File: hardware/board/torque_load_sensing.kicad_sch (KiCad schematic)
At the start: 35 parts

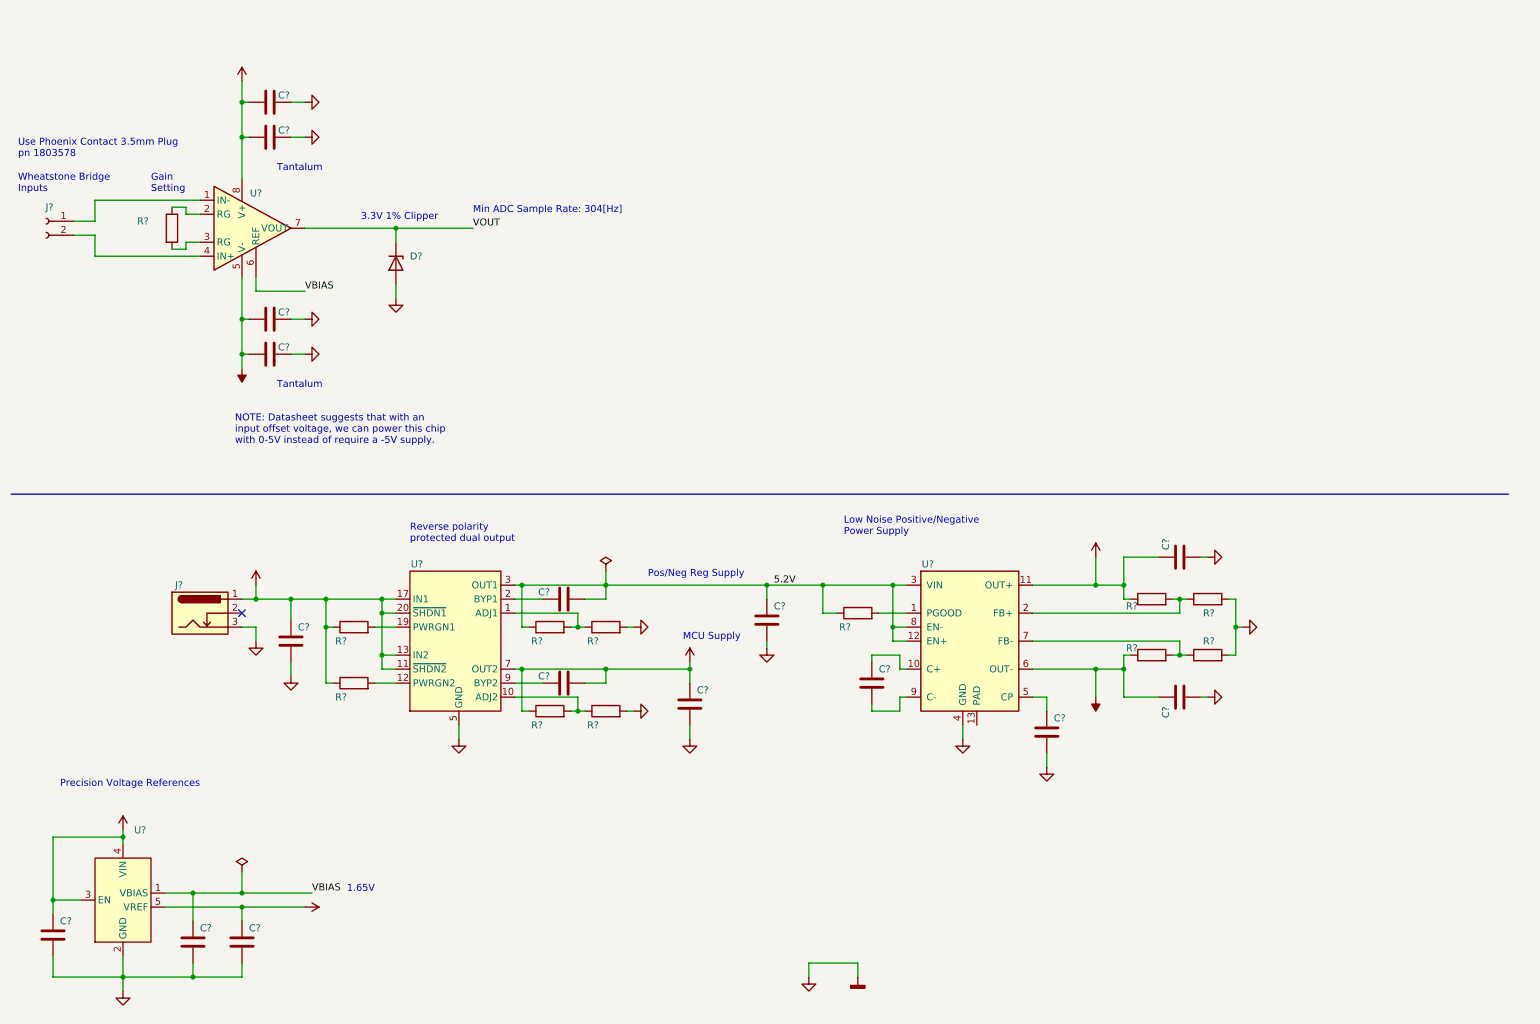
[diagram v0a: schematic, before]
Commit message: adc reading works
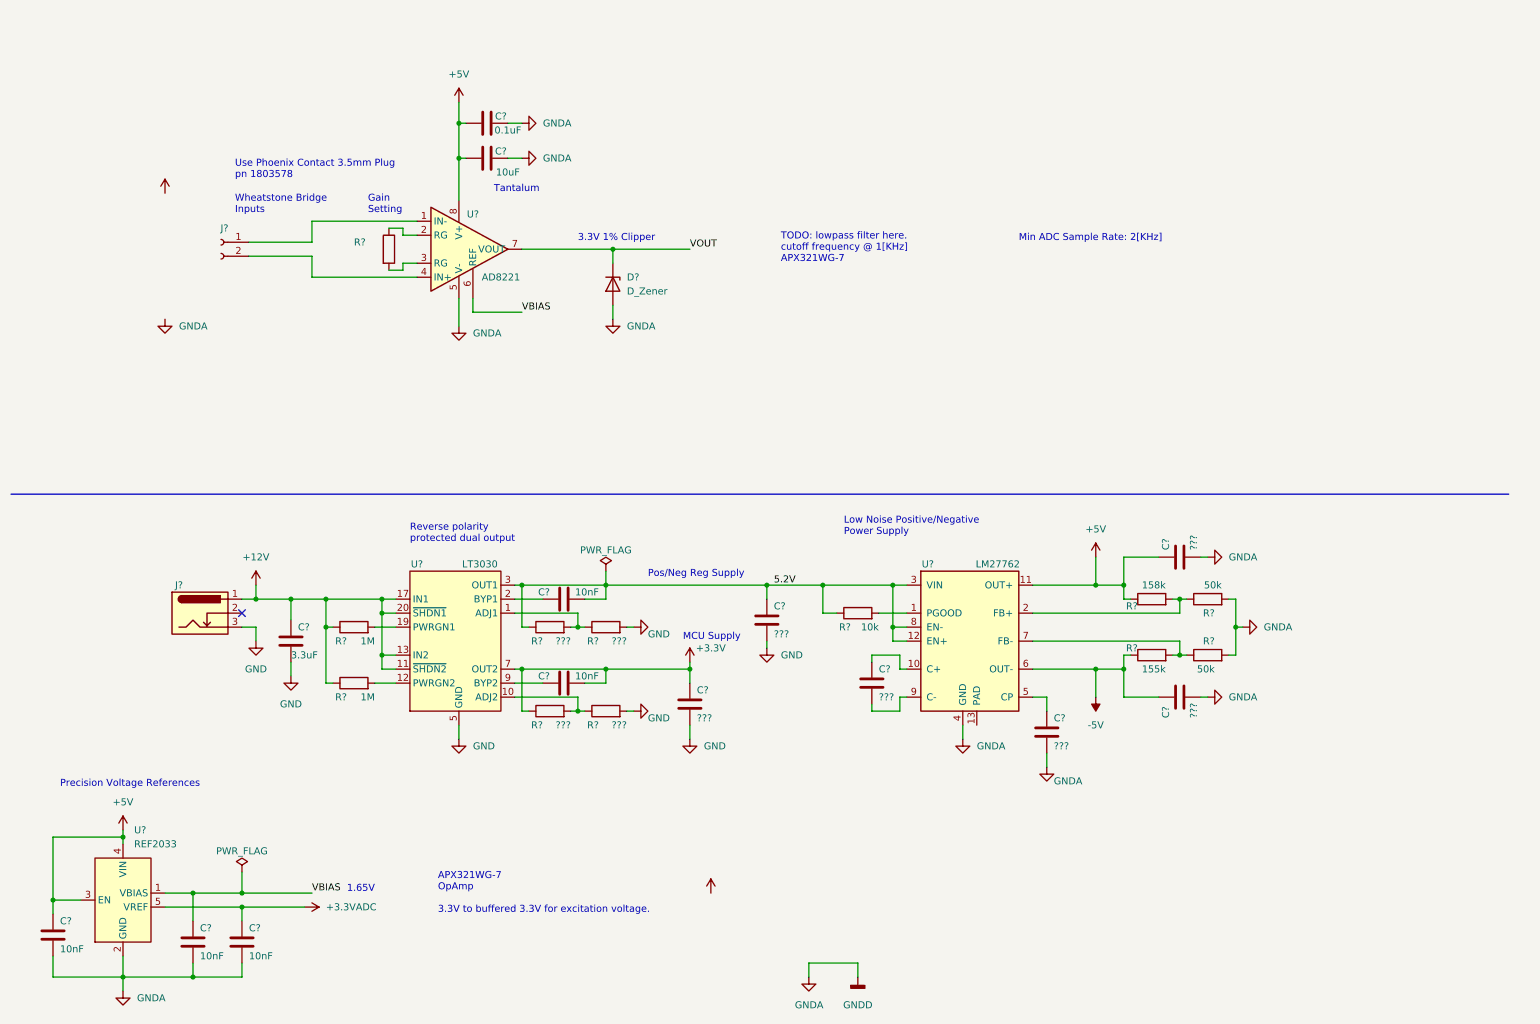
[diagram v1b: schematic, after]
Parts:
- removed C? (x2): (no value), symbol Device:C
- C? (x6), R? (x4): value (none) -> ???
- C? (x5): value (none) -> 10nF
- C?: value (none) -> 0.1uF
- C?: value (none) -> 10uF
- C?: value (none) -> 3.3uF
- D?: value (none) -> D_Zener
- J?: value (none) -> Conn_01x02_Female
- J?: value (none) -> Barrel_Jack_Switch_Pin3Ring
- R?: value (none) -> 155k
- R?: value (none) -> 158k
- R? (x2): value (none) -> 50k
- R?: value (none) -> 10k
- R? (x2): value (none) -> 1M
- U?: value (none) -> AD8221; footprint (none) -> Package_SO:MSOP-8_3x3mm_P0.65mm
- U?: value (none) -> REF2033; footprint (none) -> Package_TO_SOT_SMD:SOT-23-5
- U?: value (none) -> LT3030
- U?: value (none) -> LM27762; footprint (none) -> Package_SON:WSON-12-1EP_3x2mm_P0.5mm_EP1x2.65_ThermalVias
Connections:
- net -5V: no longer U?.5 (V-)
- net GNDA: now also U?.5 (V-)
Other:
- note added: "APX321WG-7 OpAmp 3.3V to buffered 3.3V for excitation voltage."
- note added: "Min ADC Sample Rate: 2[KHz]"
- note added: "TODO: lowpass filter here. cutoff frequency @ 1[KHz] APX321WG-7"
- note removed: "Min ADC Sample Rate: 304[Hz]"
- note removed: "NOTE: Datasheet suggests that with an input offset voltage, we can power this chip with 0-5V instead of require a -5V supply."
- moved on the sheet: C?, D?, J?, R?, U?

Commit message: debug port works; draft current driver
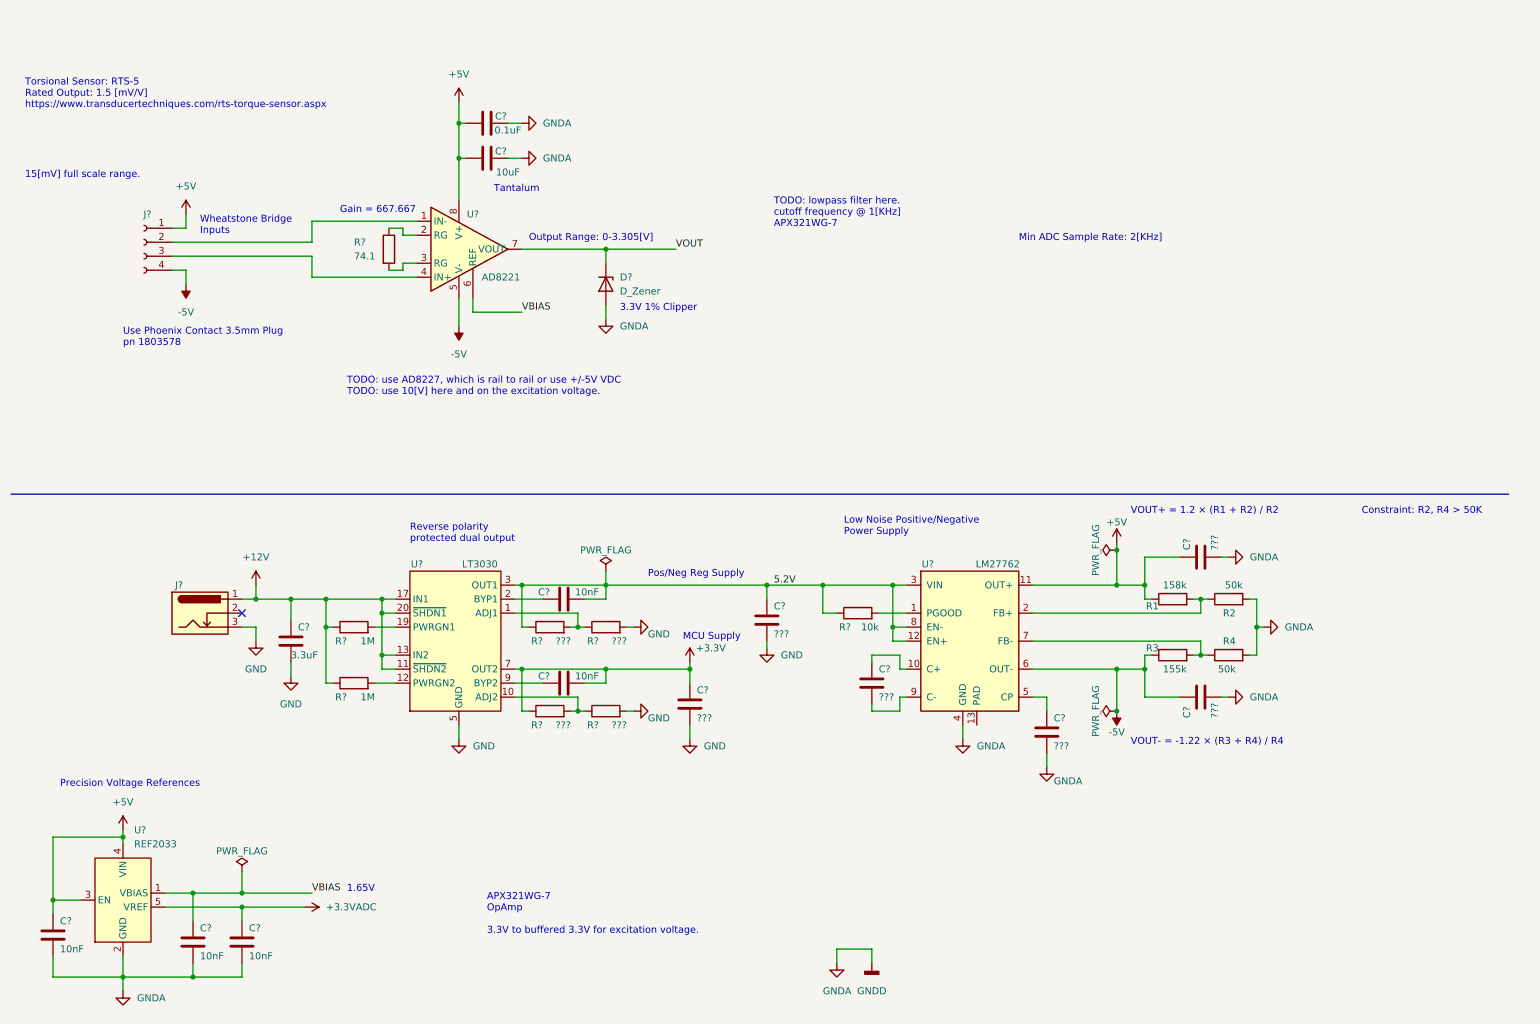
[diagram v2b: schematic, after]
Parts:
- removed J?: Conn_01x02_Female, symbol Connector:Conn_01x02_Female
- added J?: Conn_01x04_Female, symbol Connector:Conn_01x04_Female
- R?: value (none) -> 74.1; footprint (none) -> Resistor_SMD:R_0603_1608Metric; Link (none) -> https://www.mouser.com/ProductDetail/Vishay-Thin-Film/PTN06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; Manufacturer Number (none) -> PTN0603E74R1BST1
- gave numbers to parts that had none: 4
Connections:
- net +5V: now also J?.1 (Pin_1)
- net -5V: now also U?.5 (V-), J?.4 (Pin_4)
- net GNDA: no longer U?.5 (V-)
- net at U?.1 (IN-): now also J?.2 (Pin_2)
- net at U?.4 (IN+): now also J?.3 (Pin_3)
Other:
- note added: "15[mV] full scale range."
- note added: "Constraint: R2, R4 > 50K"
- note added: "Gain = 667.667"
- note added: "Output Range: 0-3.305[V]"
- note added: "TODO: use AD8227, which is rail to rail or use +/-5V VDC TODO: use 10[V] here and on the excitation voltage."
- note added: "Torsional Sensor: RTS-5 Rated Output: 1.5 [mV/V] https://www.transducertechniques.com/rts-torque-sensor.aspx"
- note added: "VOUT+ = 1.2 × (R1 + R2) / R2"
- note added: "VOUT- = -1.22 × (R3 + R4) / R4"
- note removed: "Gain Setting"
- moved on the sheet: C?, D?, R1, R2, R3, R4

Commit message: update board schematic
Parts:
- removed C? (x6): ???, symbol Device:C
- removed C? (x2): 10nF, symbol Device:C
- removed C?: 10uF, symbol Device:C
- removed C?: 3.3uF, symbol Device:C
- removed J?: Barrel_Jack_Switch_Pin3Ring, symbol Connector:Barrel_Jack_Switch_Pin3Ring
- removed J?: Conn_01x04_Female, symbol Connector:Conn_01x04_Female
- removed R1: 158k, symbol Device:R
- removed R2, R4: 50k, symbol Device:R
- removed R3: 155k, symbol Device:R
- removed R? (x4): ???, symbol Device:R
- removed R?: 10k, symbol Device:R
- removed R? (x2): 1M, symbol Device:R
- removed U?: LT3030, symbol machine_agency_components:LT3030
- removed U?: LM27762, Package_SON:WSON-12-1EP_3x2mm_P0.5mm_EP1x2.65_ThermalVias, symbol Regulator_SwitchedCapacitor:LM27762
- added C1: 300pF, Capacitor_SMD:C_0402_1005Metric, symbol Device:C
- added C2, C?: 10uF, Capacitor_SMD:C_0805_2012Metric, symbol Device:C_Polarized
- added C3: 1000pF, symbol Device:C
- added C4, C5: 100pF, symbol Device:C
- added C?: 0.1uF, symbol Device:C
- added J1: Conn_01x05_Female, symbol Connector:Conn_01x05_Female
- added R10, R11: 10K, symbol Device:R
- added R5, R6: 100, Resistor_SMD:R_0402_1005Metric, symbol Device:R
- added R7, R8, R9: 49.9, Resistor_SMD:R_0402_1005Metric, symbol Device:R
- added TP1: TestPoint, kicad_component_library:TestPoint_Keystone_5027_Miniature, symbol Connector:TestPoint
- added U1: ADS7049, Package_SO:VSSOP-8_2.3x2mm_P0.5mm, symbol Analog_ADC:ADS7049
- R?: value 74.1 -> 499
- U?: value AD8221 -> AD8226; Link (none) -> https://www.digikey.com/en/products/detail/analog-devices-i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; Manufacturer (none) -> Analog Devices Inc.; Manufacturer Number (none) -> AD8226BRMZ-R7
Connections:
- net +3V3: now also U1.1 (DVDD)
- net +5V: now also C2.2, J1.1 (Pin_1)
- net -5V: now also C?.1, C?.2, J1.4 (Pin_4)
- net GND: now also C?.2, C?.2, C?.2, U?.2 (GND), C4.2, C5.1, J1.5 (Pin_5), R6.1, U1.8 (GND)
- net GNDA: now also C2.1, C?.1, C?.2; no longer C?.2, C?.2, C?.2, U?.2 (GND)
- net at U?.1 (IN-): now also C3.1, C5.2, R10.2
- net at U?.4 (IN+): now also C3.2, C4.1, R11.1
- net +3.3VADC renamed VREF_3V3
- net VREF_3V3: now also U1.7 (AVDD)
- net VBIAS renamed VREF_1V65
- net VOUT: no longer names the net of D?.1 (K), U?.7 (VOUT)
- net VOUT: now also R5.2, TP1.1
- new net: C1.1, R5.1, U1.6 (AINP)
- new net: R9.1, U1.4 (~{CS})
- new net: R8.1, U1.2 (SCLK)
- new net: C1.2, R6.2, U1.5 (AINM)
- new net: J1.2 (Pin_2), R10.1
- new net: J1.3 (Pin_3), R11.2
- new net: R7.1, U1.3 (SDO)
- new net ADC_CS: R9.2
- new net ADC_POCI: R7.2
- new net ADC_SCK: R8.2
- no-connect marks 1 -> 0
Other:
- note added: "15[mV] full scale range with 10V excitation voltage."
- note added: "AD8226 has indefinite short-circuit current output of 13mA."
- note added: "F_{c com} = 1/(2πRC_{C}) = 159.155KHz"
- note added: "F_{c diff} = 1/(2πR(2C_{D} + C_{C})) = 7.579KHz"
- note added: "Gain = 100"
- note added: "Note: AD8226 has excellent common mode rejection, so common mode lowpass filter isn't critical."
- note added: "Note: test point output will look slightly distorted with small transient spikes when the ADS7049 is acquiring samples."
- note added: "Output Range: 0-3.3[V]"
- note added: "See Signal Chain Basics #78 for more details on common mode voltage limitations. https://www.planetanalog.com/signal-chain-basics-78-how-to-avoid-common-mode-limitations-on-instrumentation-amplifiers/"
- note added: "Shield →"
- note added: "U13 must be driven by a low impedance source and requires ~300pF input capacitance for stability."
- note removed: "1.65V"
- note removed: "15[mV] full scale range."
- note removed: "APX321WG-7 OpAmp 3.3V to buffered 3.3V for excitation voltage."
- note removed: "Constraint: R2, R4 > 50K"
- note removed: "Gain = 667.667"
- note removed: "Low Noise Positive/Negative Power Supply"
- note removed: "MCU Supply"
- note removed: "Min ADC Sample Rate: 2[KHz]"
- note removed: "Output Range: 0-3.305[V]"
- note removed: "Pos/Neg Reg Supply"
- note removed: "Reverse polarity protected dual output"
- note removed: "TODO: lowpass filter here. cutoff frequency @ 1[KHz] APX321WG-7"
- note removed: "TODO: use AD8227, which is rail to rail or use +/-5V VDC TODO: use 10[V] here and on the excitation voltage."
- note removed: "VOUT+ = 1.2 × (R1 + R2) / R2"
- note removed: "VOUT- = -1.22 × (R3 + R4) / R4"
- moved on the sheet: C?, D?, R?, U?

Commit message: update pcb
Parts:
- removed C? (x3): 10nF, symbol Device:C
- removed U?: REF2033, Package_TO_SOT_SMD:SOT-23-5, symbol machine_agency_components:REF20xx
- renumbered C4 to C?, C1 to C?, C3 to C?, C5 to C?, C2 to C?, J1 to J?, R5 to R?, R9 to R?, R8 to R?, R6 to R?, R11 to R?, R10 to R?, R7 to R?, U1 to U?
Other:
- note removed: "Precision Voltage References"
- moved on the sheet: C?, R?, TP1, U?
